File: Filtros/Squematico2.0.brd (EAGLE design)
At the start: 32 x 20.6 mm, 8 parts, among them IC1 LM358N

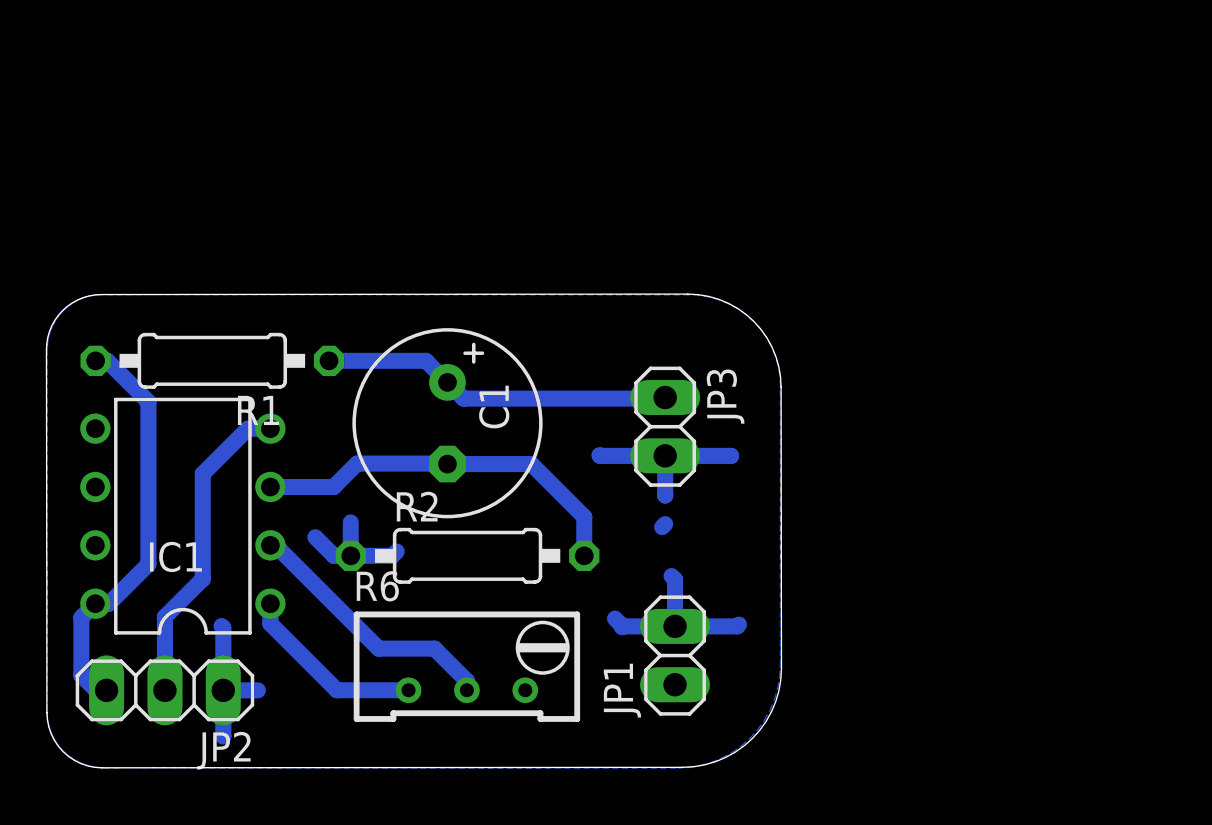
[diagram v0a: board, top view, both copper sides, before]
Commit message: Se agregan pistas para los filtros y se crean los comparadores
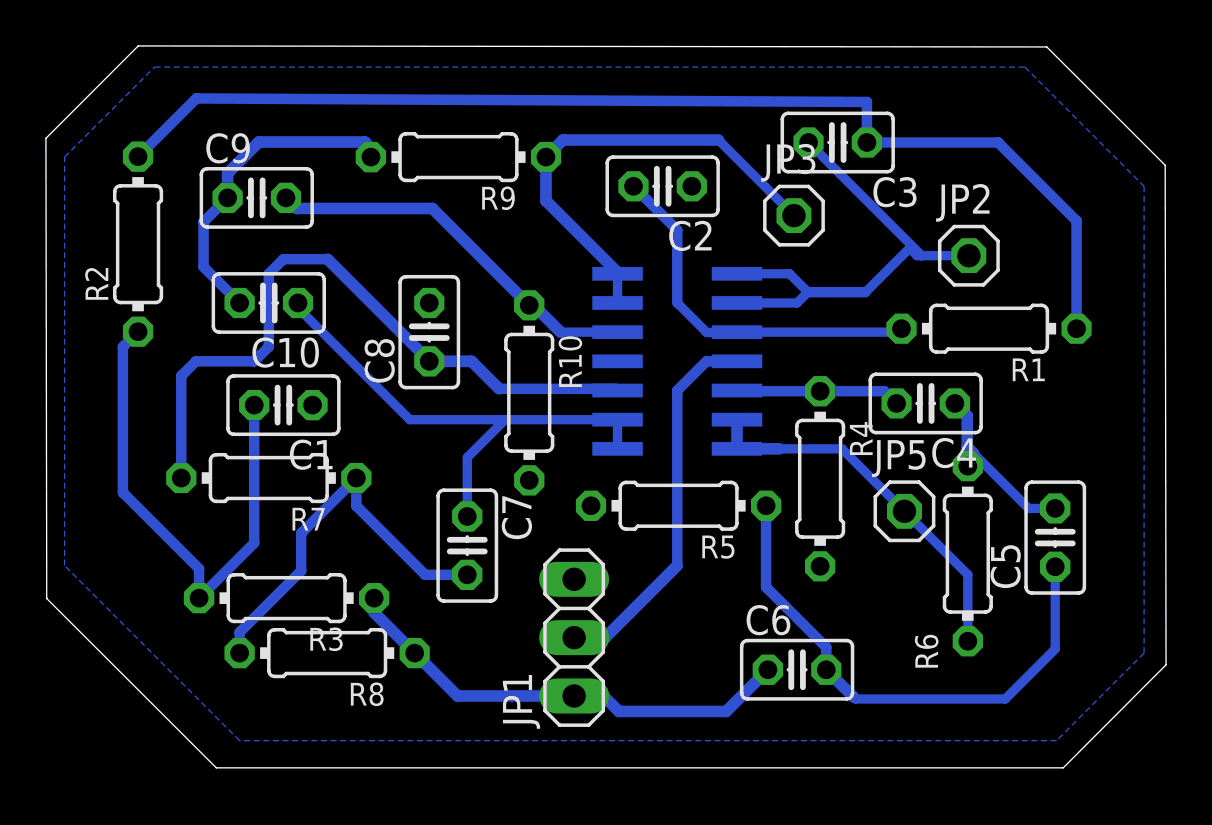
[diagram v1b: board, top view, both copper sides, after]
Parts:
- added C10, C2, C3, C4, C5, C6, C7, C8, C9: (no value), rcl:C025-025X050
- added JP5: (no value), pinhead:1X01
- added R10, R3, R4, R5, R7, R8, R9: (no value), rcl:0204/7
- C1: value 4.7u -> (none); device rcl:E3,5-8 -> rcl:C025-025X050
- IC1: value LM358N -> LM324D; device linear:DIL08 -> linear:SO14
- JP1: device pinhead:1X02 -> pinhead:1X03
- JP2: device pinhead:1X03 -> pinhead:1X01
- JP3: device pinhead:1X02 -> pinhead:1X01
- R1: value 2.2k -> (none); device rcl:0207/10 -> rcl:0204/7
- R2: value 10k -> (none); device rcl:0207/10 -> rcl:0204/7
- R6: device rcl:RTRIM64W -> rcl:0204/7
- moved JP2 39.8 mm to (40.1, 22.3), turned to 0 degrees
- moved R1 33.8 mm to (41.0, 19.1)
- moved IC1 22.6 mm to (27.4, 17.7), flipped to the bottom, turned to 270 degrees
- moved R6 22.3 mm to (40.1, 9.32), turned to 90 degrees
- moved R2 19.7 mm to (3.96, 22.8), turned to 90 degrees
- moved JP3 10.8 mm to (32.5, 24.0), turned to 0 degrees
- moved C1 7.19 mm to (10.3, 15.8), turned to 180 degrees
- moved JP1 4.46 mm to (22.9, 5.67)
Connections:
- removed net 0: JP1.2, JP2.1, JP3.2, R2.1, R6.3
- removed net V+: IC1.8, JP2.3, R1.2
- removed net V-: IC1.4, JP2.2
- removed net VAMP: IC1.1, JP1.1, R6.1
- removed net VO: C1.-, IC1.3, R2.2
- new net BAND_1: C10.1, C7.1, IC1.8, IC1.9
- new net BAND_T1: IC1.13, IC1.14, JP3.1, R9.1
- new net GND: C1.1, C2.1, C8.2, IC1.11, JP1.3, R10.2, R4.2, R5.2
- new net HIGH: IC1.6, IC1.7, JP5.1, R6.1
- new net IN: C6.1, JP1.1, R3.1, R8.1
- new net LOW: C3.2, IC1.1, IC1.2, JP2.1
- new net N$11: C9.2, IC1.12, R10.1
- new net N$14: C10.2, C9.1, R9.2
- new net N$3: C1.2, R2.1, R3.2
- new net N$4: C4.2, IC1.5, R4.1
- new net N$6: C4.1, C5.2, R6.2
- new net N$7: C5.1, C6.2, R5.1
- new net N$8: C7.2, R7.1, R8.2
- new net N$9: C8.1, IC1.10, R7.2
- new net VCC: IC1.4, JP1.2
- net N$1: now also C2.2, IC1.3, R1.2; no longer C1.+, JP3.1, R1.1
- net N$2: now also C3.1, R1.1, R2.2; no longer IC1.2, R6.2
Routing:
- net N$2: track 11.4 -> 49.8 mm
- net N$9: track 0.00 -> 29.8 mm
- net 0: track 27.3 -> 0.00 mm
- net N$7: track 0.00 -> 23.2 mm
- net N$3: track 0.00 -> 22.6 mm
- net BAND_1: track 0.00 -> 22.3 mm
- net LOW: track 0.00 -> 21.6 mm
- net IN: track 0.00 -> 20.3 mm
- net BAND_T1: track 0.00 -> 20.1 mm
- net V+: track 17.9 -> 0.00 mm
- net N$8: track 0.00 -> 17.0 mm
- net N$11: track 0.00 -> 16.9 mm
- net VO: track 16.7 -> 0.00 mm
- net VCC: track 0.00 -> 16.5 mm
- net HIGH: track 0.00 -> 16.5 mm
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- added copper zone on layer 16, net GND
- removed copper zone on layer 16, net 0
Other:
- board size 32 x 20.6 mm -> 48.8 x 31.4 mm

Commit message: Se agregan conexiones y archivos de configuración CNC
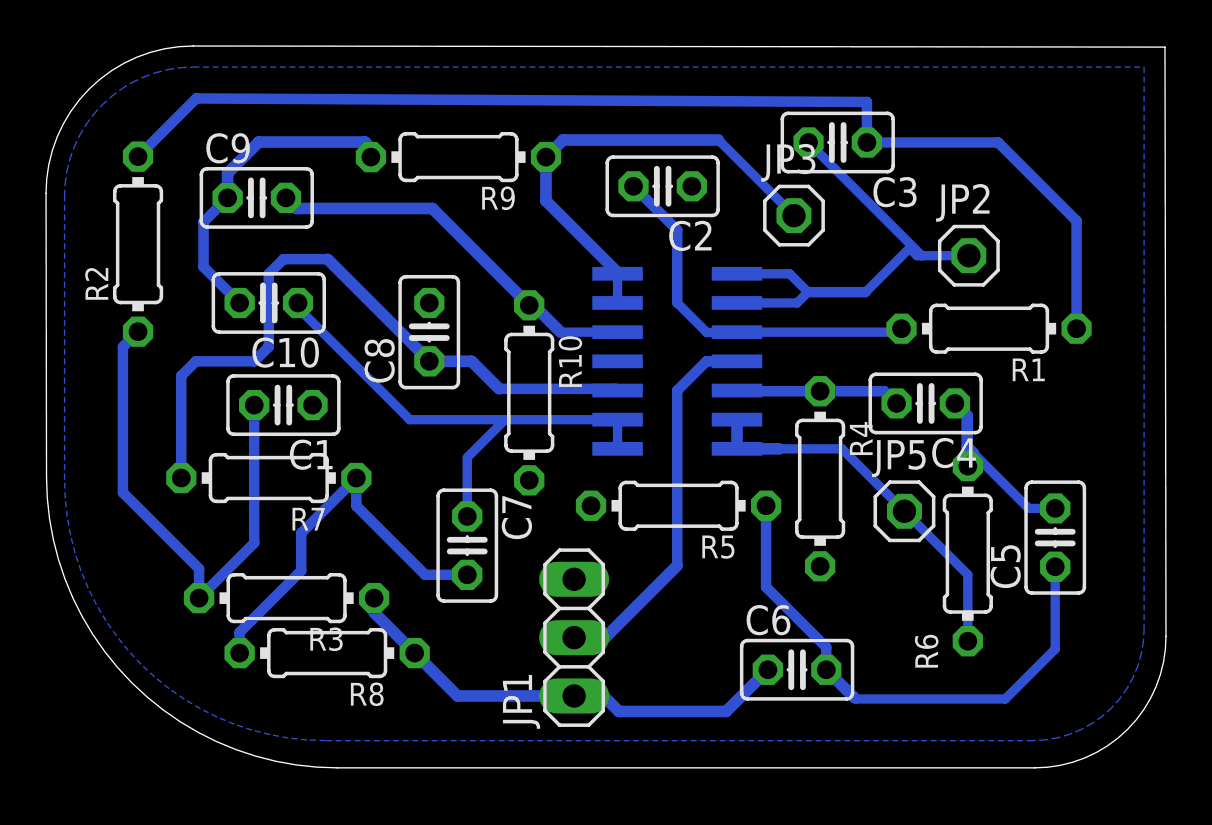
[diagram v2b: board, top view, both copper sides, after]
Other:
- outline, holes or cut-outs redrawn
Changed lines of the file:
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@@
 <board>
 <plain>
-<wire x1="-0.046953125" y1="27.4031375" x2="-0.012628125" y2="7.370121875" width="0" layer="20"/>
-<wire x1="-0.012628125" y1="7.370121875" x2="7.36924375" y2="0" width="0" layer="20"/>
-<wire x1="7.36924375" y1="0" x2="44.23346875" y2="0" width="0" layer="20"/>
-<wire x1="44.23346875" y1="0" x2="48.70948125" y2="4.484309375" width="0" layer="20"/>
-<wire x1="48.70948125" y1="4.484309375" x2="48.67215625" y2="26.23038125" width="0" layer="20"/>
-<wire x1="48.67215625" y1="26.23038125" x2="43.519590625" y2="31.379534375" width="0" layer="20"/>
-<wire x1="43.519590625" y1="31.379534375" x2="3.970615625" y2="31.423834375" width="0" layer="20"/>
-<wire x1="3.970615625" y1="31.423834375" x2="-0.046953125" y2="27.4031375" width="0" layer="20"/>
+<wire x1="12.6386125" y1="0" x2="42.9944625" y2="0" width="0" layer="20"/>
+<wire x1="42.9944625" y1="0" x2="48.70735625" y2="5.7223625" width="0" layer="20" curve="90.09487"/>
+<wire x1="48.70735625" y1="5.7223625" x2="48.663328125" y2="31.373771875" width="0" layer="20"/>
+<wire x1="48.663328125" y1="31.373771875" x2="6.367328125" y2="31.42115" width="0" layer="20"/>
+<wire x1="6.367328125" y1="31.42115" x2="-0.042846875" y2="25.006615625" width="0" layer="20" curve="90.171644"/>
+<wire x1="-0.042846875" y1="25.006615625" x2="-0.02165625" y2="12.639184375" width="0" layer="20"/>
+<wire x1="-0.02165625" y1="12.639184375" x2="12.6386125" y2="0" width="0" layer="20" curve="89.901822"/>
 </plain>
 <attributes>
@@
 <contactref element="C8" pad="2"/>
 <polygon width="0.508" layer="16" orphans="yes">
-<vertex x="4.6829" y="30.50463125"/>
-<vertex x="42.5646" y="30.50463125"/>
-<vertex x="47.75375" y="25.31548125"/>
-<vertex x="47.75375" y="4.99548125"/>
-<vertex x="43.94375" y="1.18548125"/>
-<vertex x="8.38375" y="1.18548125"/>
-<vertex x="0.76375" y="8.80548125"/>
-<vertex x="0.76375" y="26.58548125"/>
+<vertex x="42.905746875" y="1.18548125"/>
+<vertex x="12.12141875" y="1.18548125" curve="-90"/>
+<vertex x="0.76375" y="12.54315"/>
+<vertex x="0.76375" y="24.896928125" curve="-90"/>
+<vertex x="6.371453125" y="30.50463125"/>
+<vertex x="47.75375" y="30.50463125"/>
+<vertex x="47.75375" y="6.033484375" curve="-90"/>
 </polygon>
 </signal>
